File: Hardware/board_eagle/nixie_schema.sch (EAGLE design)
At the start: 230 parts, among them J2 RTC_CONSMD, J4 RTC_CONTHT, P1 100k, P2 10k, Q1 BC856B, Q3 BC856B, Q4 BCX70H, Q5 NTF5P03, T1 PHOTO_TRANS, U2 MC7940N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

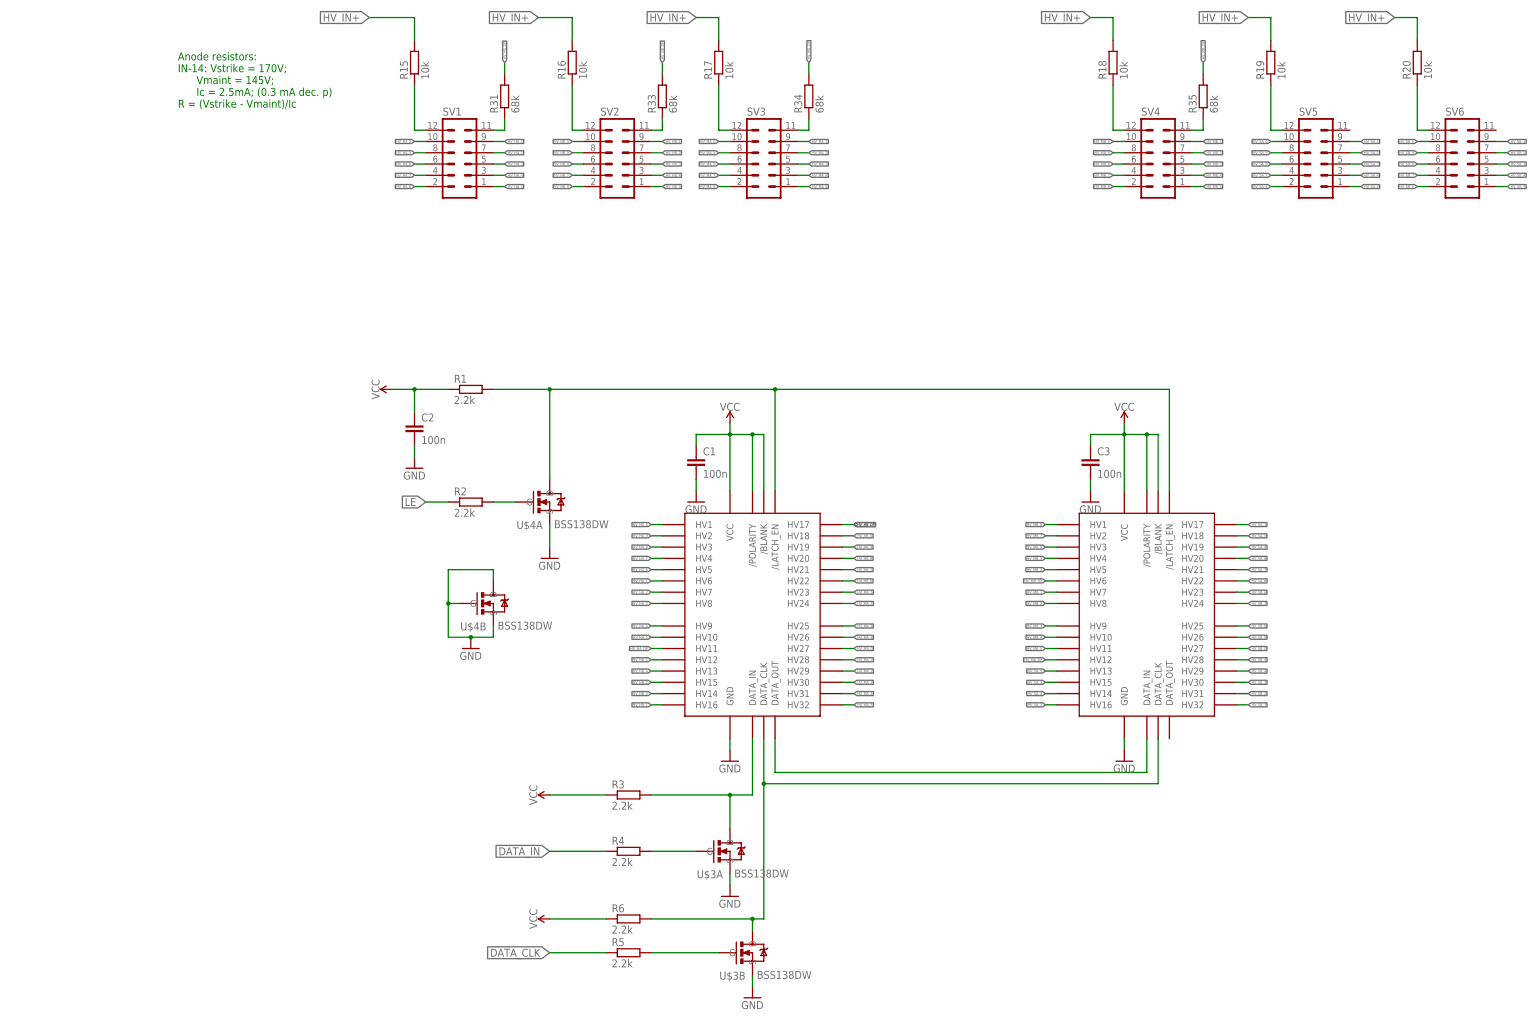
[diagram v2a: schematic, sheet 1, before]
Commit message: Bottom board routing. Some DRC errors remain.
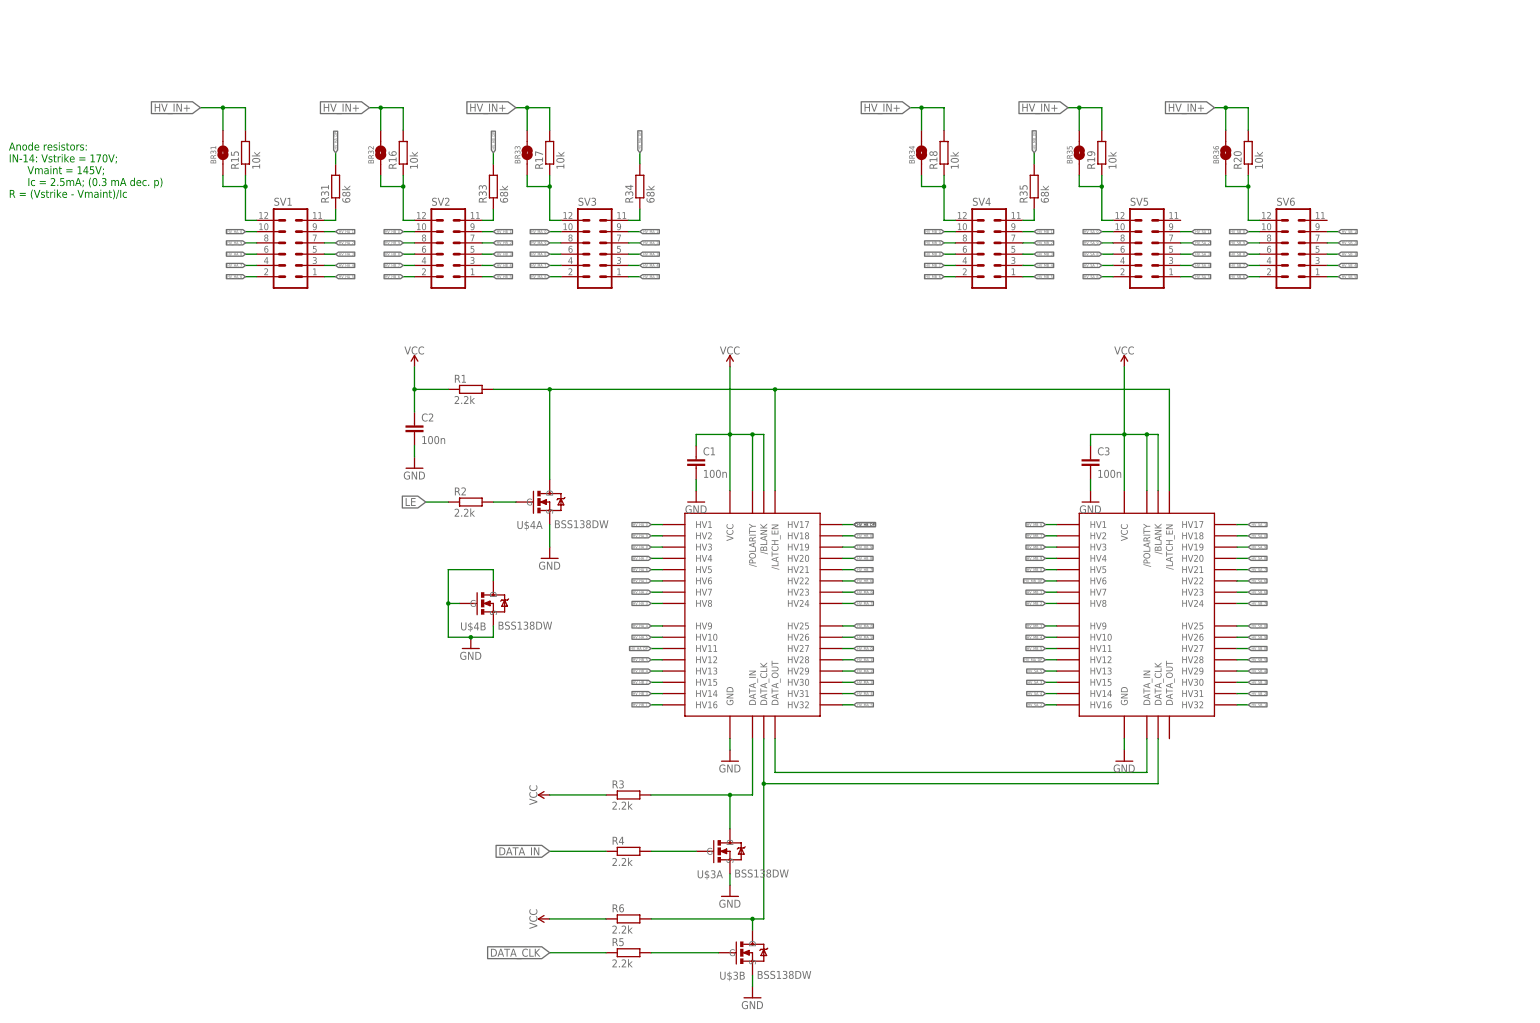
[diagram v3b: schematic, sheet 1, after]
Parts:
- added BR31, BR32, BR33, BR34, BR35, BR36: HV_SOLDER_BRIDGE, nixe_cmp:HV_SOLDER_BRIDGE
- P2: value 10k -> 100k
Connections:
- net HV_IN+: now also BR31.2, BR32.2, BR33.2, BR34.2, BR35.2, BR36.2
- net N$11: now also BR33.1
- net N$8: now also BR34.1
- net N$89: now also BR31.1
- net N$90: now also BR32.1
- net N$91: now also BR36.1
- net N$92: now also BR35.1
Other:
- moved on the sheet: R15, R16, R17, R18, R19, R20, R31, R33, R34, R35, SV1, SV2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

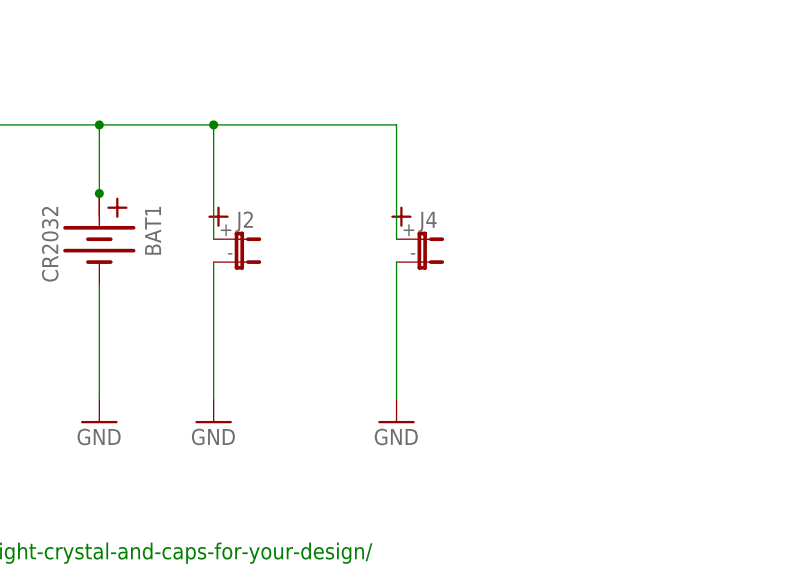
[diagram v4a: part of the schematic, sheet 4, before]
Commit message: Silk screen touch ups
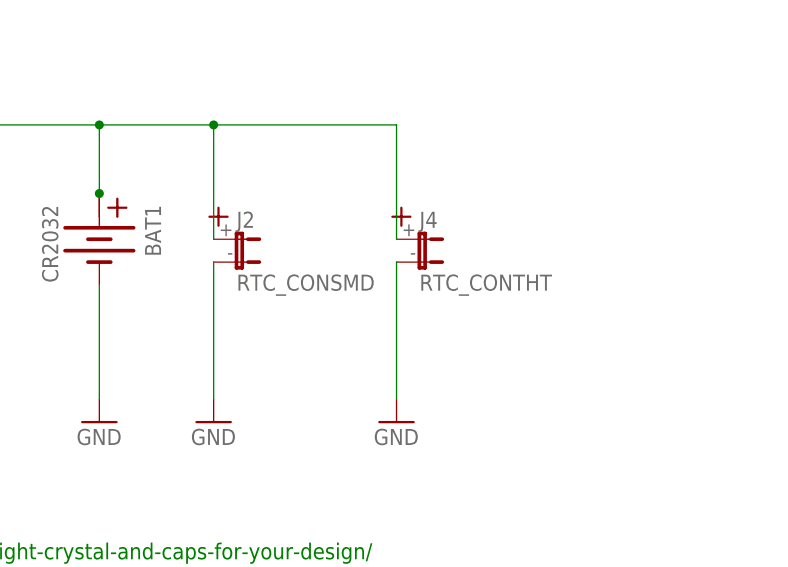
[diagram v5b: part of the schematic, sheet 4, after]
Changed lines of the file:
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@@
 <part name="Y1" library="nixe_cmp" deviceset="ECS-.327-7-34B" device="" value=""/>
 <part name="BAT1" library="nixe_cmp" deviceset="CR2032" device=""/>
-<part name="J2" library="nixe_cmp" deviceset="RTC_CON" device="SMD" value=""/>
-<part name="J4" library="nixe_cmp" deviceset="RTC_CON" device="THT" value=""/>
+<part name="J2" library="nixe_cmp" deviceset="RTC_CON" device="SMD" value="RTC_CONSMD"/>
+<part name="J4" library="nixe_cmp" deviceset="RTC_CON" device="THT" value="RTC_CONTHT"/>
 <part name="GND16" library="supply1" library_urn="urn:adsk.eagle:library:371" deviceset="GND" device=""/>
 <part name="GND17" library="supply1" library_urn="urn:adsk.eagle:library:371" deviceset="GND" device=""/>
